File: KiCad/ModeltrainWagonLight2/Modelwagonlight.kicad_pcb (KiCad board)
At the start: 2 copper layers, 25 x 11 mm, 17 parts, among them J1 Conn_01x01, J2 Conn_01x01, J3 Conn_01x01, J4 Conn_01x01, U1 LP2951DR

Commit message: Update om light2
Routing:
- net Net-(C1-Pad2): track 48.5 -> 57.7 mm
- net Net-(C2-Pad1): track 26.0 -> 30.0 mm
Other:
- rule via_min_size: 0.4 -> 0.5
- board text added: "+LED-"

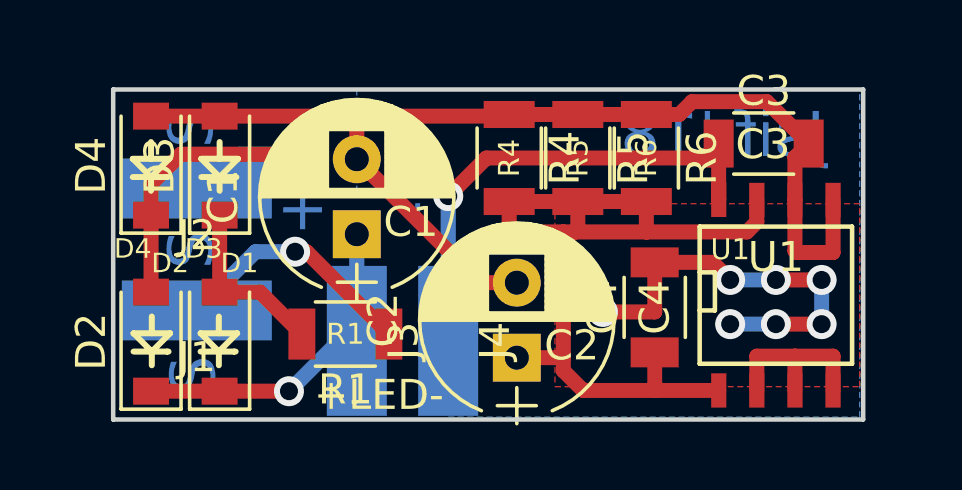
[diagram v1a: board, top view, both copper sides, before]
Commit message: Updated all schematics and layouts. Updated all component lists and csv files. Created ShopCartAll.csv from farnell big order for these 4 boards. Created new gerber files in the board-named directories to be send to PCB farmer.
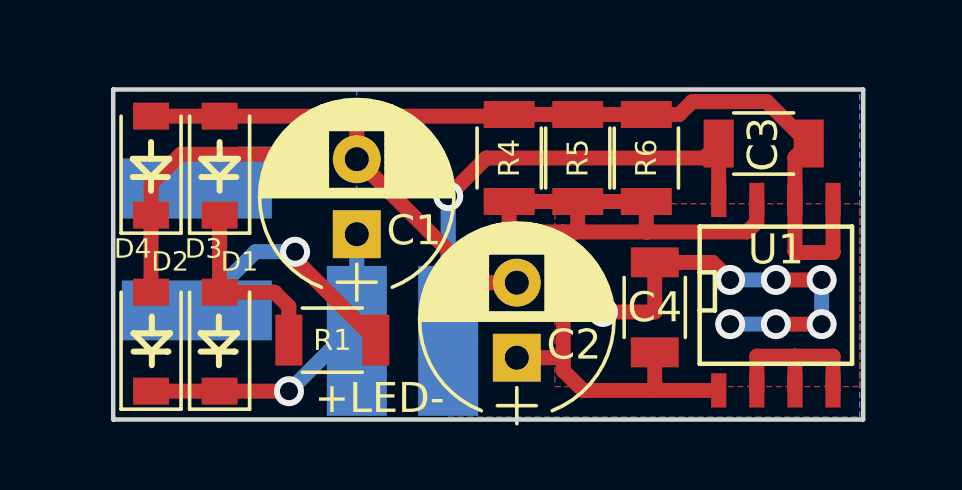
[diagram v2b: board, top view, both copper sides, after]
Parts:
- moved R1 0.48 mm to (197.3, 119.4)
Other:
- board text added: "Jsif 2019 WagonLight"
- board text removed: "Jsif '18"
- board text removed: "U1"
